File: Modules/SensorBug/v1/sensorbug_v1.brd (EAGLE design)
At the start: 41 x 30 mm, 43 parts, among them IC1 MX25R8035FZUIL0, T2 DMP3010LK3

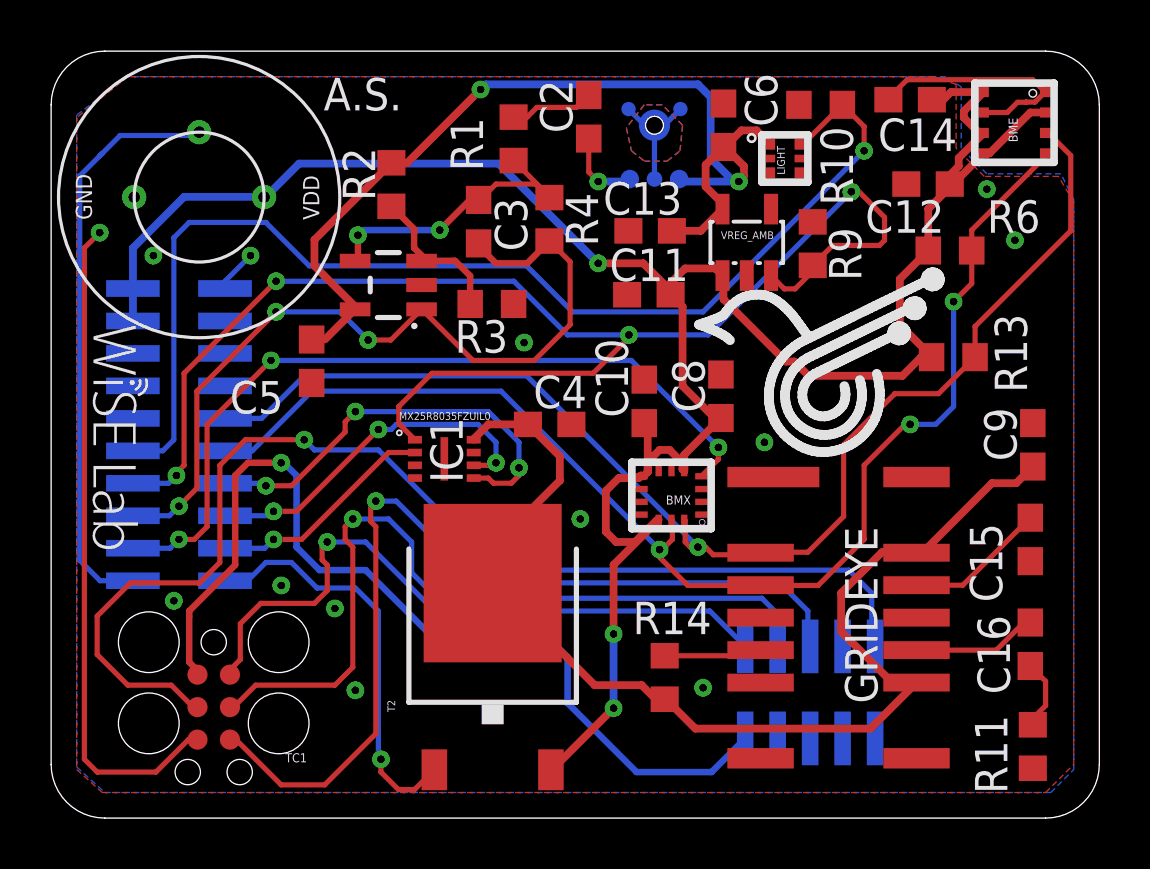
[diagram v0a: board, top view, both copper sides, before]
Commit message: Fixed Light Sensor Output
Previous light sensor output pin did not have ADC capabilities.
Interchanged DOMAIN1_EN and LIGHT_OUT.
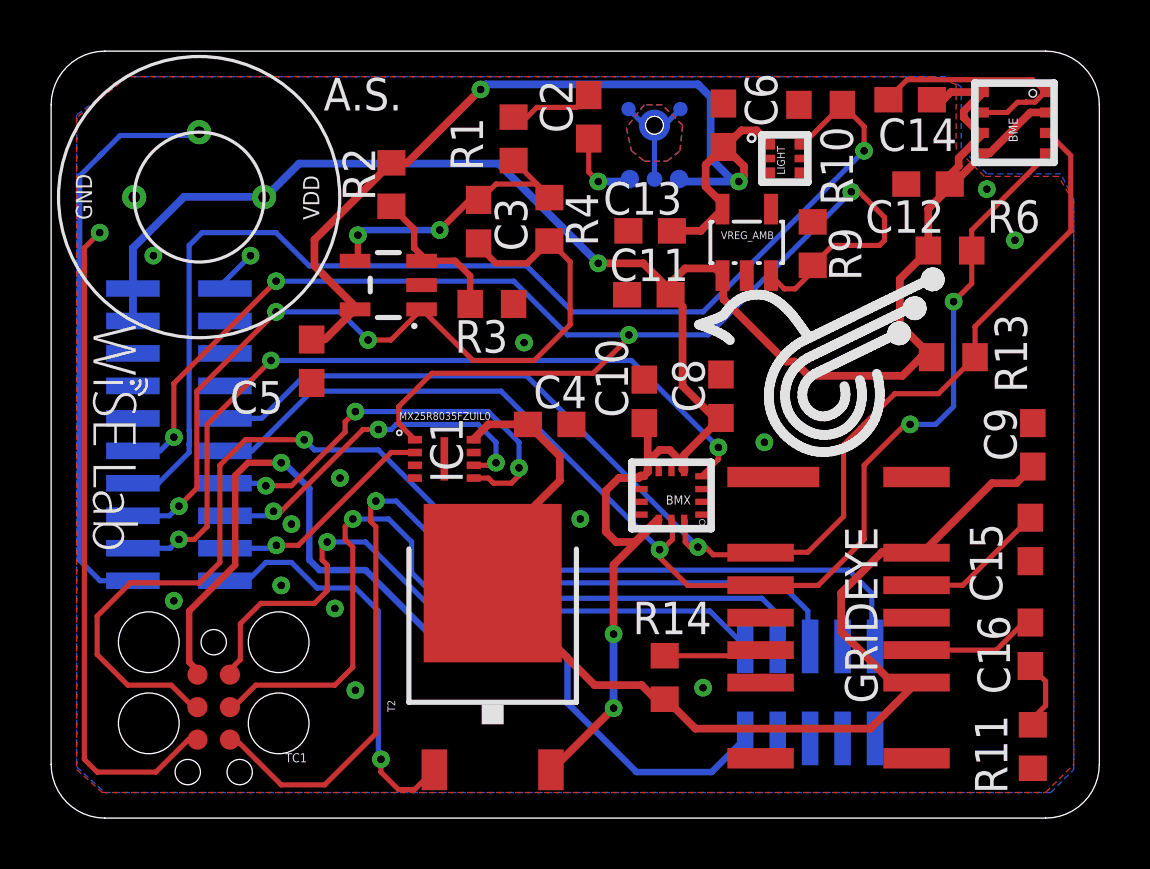
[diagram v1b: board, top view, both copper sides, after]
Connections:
- net DOMAIN1_EN: now also U$4.11; no longer U$4.13
- net LIGHT_OUT: now also U$4.13; no longer U$4.11
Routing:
- net DOMAIN1_EN: track 56.7 -> 55.2 mm
- net GND: vias 13 -> 15
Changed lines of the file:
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@@
 <layers>
 <layer number="1" name="Top" color="4" fill="1" visible="yes" active="yes"/>
-<layer number="16" name="Bottom" color="1" fill="1" visible="no" active="yes"/>
+<layer number="16" name="Bottom" color="1" fill="1" visible="yes" active="yes"/>
 <layer number="17" name="Pads" color="2" fill="1" visible="yes" active="yes"/>
 <layer number="18" name="Vias" color="2" fill="1" visible="yes" active="yes"/>
@@
 <via x="4" y="22" extent="1-16" drill="0.3"/>
 <via x="20.7" y="11.7" extent="1-16" drill="0.3"/>
+<via x="11.3" y="13.3" extent="1-16" drill="0.3"/>
+<via x="9.4" y="11.5" extent="1-16" drill="0.3"/>
 </signal>
 <signal name="SDA">
@@
 <wire x1="8.525" y1="11.825" x2="8.7" y2="12" width="0.2032" layer="16"/>
 <via x="8.7" y="12" extent="1-16" drill="0.3"/>
-<wire x1="8.7" y1="12" x2="9.6" y2="12" width="0.2032" layer="1"/>
-<wire x1="9.6" y1="12" x2="12.8" y2="15.2" width="0.2032" layer="1"/>
 <via x="12.8" y="15.2" extent="1-16" drill="0.3"/>
 <wire x1="12.8" y1="15.2" x2="13.3" y2="15.2" width="0.2032" layer="16"/>
@@
 <wire x1="17.2" y1="13.9" x2="17.1" y2="13.8" width="0.2032" layer="1"/>
 <wire x1="17.1" y1="13.8" x2="16.53" y2="13.8" width="0.2032" layer="1"/>
+<wire x1="8.7" y1="12" x2="9" y2="12" width="0.2032" layer="1"/>
+<wire x1="9" y1="12" x2="12.2" y2="15.2" width="0.2032" layer="1"/>
+<wire x1="12.2" y1="15.2" x2="12.8" y2="15.2" width="0.2032" layer="1"/>
 </signal>
 <signal name="MISO">
 <contactref element="IC1" pad="2"/>
 <contactref element="U$4" pad="18"/>
-<wire x1="6.8" y1="10.555" x2="8.355" y2="10.555" width="0.2032" layer="16"/>
-<wire x1="8.355" y1="10.555" x2="8.7" y2="10.9" width="0.2032" layer="16"/>
-<via x="8.7" y="10.9" extent="1-16" drill="0.3"/>
-<wire x1="8.7" y1="10.9" x2="9.8" y2="10.9" width="0.2032" layer="1"/>
-<wire x1="9.8" y1="10.9" x2="13.2" y2="14.3" width="0.2032" layer="1"/>
-<wire x1="13.2" y1="14.3" x2="14.23" y2="14.3" width="0.2032" layer="1"/>
+<via x="8.81" y="10.67" extent="1-16" drill="0.3"/>
+<wire x1="6.8" y1="10.555" x2="8.695" y2="10.555" width="0.2032" layer="16"/>
+<wire x1="8.695" y1="10.555" x2="8.81" y2="10.67" width="0.2032" layer="16"/>
+<wire x1="8.81" y1="10.67" x2="9.67" y2="10.67" width="0.2032" layer="1"/>
+<wire x1="9.67" y1="10.67" x2="13.3" y2="14.3" width="0.2032" layer="1"/>
+<wire x1="13.3" y1="14.3" x2="14.23" y2="14.3" width="0.2032" layer="1"/>
 </signal>
 <signal name="MOSI">
@@
 <wire x1="5.725" y1="5.61" x2="5.725" y2="5.775" width="0.254" layer="1"/>
 <wire x1="5.725" y1="5.775" x2="5.4" y2="6.1" width="0.254" layer="1"/>
-<wire x1="5.4" y1="6.1" x2="5.4" y2="7.9" width="0.254" layer="1"/>
+<wire x1="5.4" y1="6.1" x2="5.4" y2="8.1" width="0.254" layer="1"/>
 <via x="9" y="13.9" extent="1-16" drill="0.3"/>
-<wire x1="9" y1="13.9" x2="9.1" y2="13.9" width="0.254" layer="16"/>
-<wire x1="9.1" y1="13.9" x2="9.6" y2="13.4" width="0.254" layer="16"/>
-<wire x1="9.6" y1="13.4" x2="9.6" y2="10.6" width="0.254" layer="16"/>
-<wire x1="9.6" y1="10.6" x2="10.5" y2="9.7" width="0.254" layer="16"/>
-<wire x1="10.5" y1="9.7" x2="12.3" y2="9.7" width="0.254" layer="16"/>
+<wire x1="9.1" y1="13.9" x2="9" y2="13.9" width="0.254" layer="16"/>
 <wire x1="12.3" y1="9.7" x2="14.7" y2="7.3" width="0.254" layer="16"/>
 <wire x1="14.7" y1="7.3" x2="19.2" y2="7.3" width="0.254" layer="16"/>
@@
 <wire x1="22.9" y1="1.8" x2="25.8326" y2="1.8" width="0.254" layer="16"/>
 <wire x1="25.8326" y1="1.8" x2="27.1488" y2="3.1162" width="0.254" layer="16"/>
-<wire x1="5.4" y1="7.9" x2="5.4" y2="8.1" width="0.254" layer="1"/>
 <wire x1="7.2" y1="9.9" x2="5.4" y2="8.1" width="0.254" layer="1"/>
 <wire x1="7.2" y1="9.9" x2="7.2" y2="13.4" width="0.254" layer="1"/>
 <wire x1="7.2" y1="13.4" x2="7.7" y2="13.9" width="0.254" layer="1"/>
 <wire x1="7.7" y1="13.9" x2="9" y2="13.9" width="0.254" layer="1"/>
+<wire x1="9" y1="13.9" x2="9.1" y2="13.9" width="0.254" layer="16"/>
+<wire x1="9.1" y1="13.9" x2="10.1" y2="12.9" width="0.254" layer="16"/>
+<wire x1="10.1" y1="12.9" x2="10.1" y2="10.1" width="0.254" layer="16"/>
+<wire x1="10.1" y1="10.1" x2="10.5" y2="9.7" width="0.254" layer="16"/>
+<wire x1="10.5" y1="9.7" x2="12.3" y2="9.7" width="0.254" layer="16"/>
 </signal>
 <signal name="JTAG_TMS">
@@
 <wire x1="29.1" y1="20.7" x2="28.68" y2="20.7" width="0.2032" layer="1"/>
 <wire x1="28.68" y1="20.7" x2="28.16" y2="21.22" width="0.2032" layer="1"/>
-<contactref element="U$4" pad="13"/>
-<wire x1="3.2" y1="13.095" x2="4.595" y2="13.095" width="0.2032" layer="16"/>
-<wire x1="4.595" y1="13.095" x2="4.9" y2="13.4" width="0.2032" layer="16"/>
-<via x="4.9" y="13.4" extent="1-16" drill="0.3"/>
-<wire x1="4.9" y1="13.4" x2="4.9" y2="13.5" width="0.2032" layer="1"/>
-<wire x1="4.9" y1="13.5" x2="5.2" y2="13.8" width="0.2032" layer="1"/>
-<wire x1="5.2" y1="13.8" x2="5.2" y2="17.4" width="0.2032" layer="1"/>
-<wire x1="5.2" y1="17.4" x2="8.8" y2="21" width="0.2032" layer="1"/>
 <via x="8.8" y="21" extent="1-16" drill="0.3"/>
 <via x="31.3" y="24.5" extent="1-16" drill="0.3"/>
@@
 <wire x1="13.6" y1="16.1" x2="13.6" y2="15.43" width="0.2032" layer="1"/>
 <wire x1="13.6" y1="15.43" x2="14.23" y2="14.8" width="0.2032" layer="1"/>
+<contactref element="U$4" pad="11"/>
+<via x="4.8" y="14.9" extent="1-16" drill="0.3"/>
+<wire x1="3.2" y1="14.365" x2="4.265" y2="14.365" width="0.2032" layer="16"/>
+<wire x1="4.265" y1="14.365" x2="4.8" y2="14.9" width="0.2032" layer="16"/>
+<wire x1="4.8" y1="14.9" x2="4.8" y2="17" width="0.2032" layer="1"/>
+<wire x1="4.8" y1="17" x2="8.8" y2="21" width="0.2032" layer="1"/>
 </signal>
 <signal name="VREG_1">
@@
 <contactref element="LIGHT" pad="6IOUT"/>
 <contactref element="R10" pad="2"/>
-<contactref element="U$4" pad="11"/>
-<wire x1="3.2" y1="14.365" x2="4.365" y2="14.365" width="0.2032" layer="16"/>
-<wire x1="4.365" y1="14.365" x2="4.8" y2="14.8" width="0.2032" layer="16"/>
-<wire x1="4.8" y1="14.8" x2="4.8" y2="22.7" width="0.2032" layer="16"/>
-<wire x1="4.8" y1="22.7" x2="5.4" y2="23.3" width="0.2032" layer="16"/>
-<wire x1="5.4" y1="23.3" x2="8.4" y2="23.3" width="0.2032" layer="16"/>
-<wire x1="8.4" y1="23.3" x2="10.1" y2="21.6" width="0.2032" layer="16"/>
 <wire x1="10.1" y1="21.6" x2="18.6" y2="21.6" width="0.2032" layer="16"/>
 <wire x1="18.6" y1="21.6" x2="20.4" y2="19.8" width="0.2032" layer="16"/>
@@
 <wire x1="29.265" y1="26.36" x2="29.41" y2="26.36" width="0.2032" layer="1"/>
 <wire x1="29.41" y1="26.36" x2="30.95" y2="27.9" width="0.2032" layer="1"/>
+<contactref element="U$4" pad="13"/>
+<wire x1="3.2" y1="13.095" x2="4.195" y2="13.095" width="0.2032" layer="16"/>
+<wire x1="4.195" y1="13.095" x2="5.4" y2="14.3" width="0.2032" layer="16"/>
+<wire x1="5.4" y1="14.3" x2="5.4" y2="14.6" width="0.2032" layer="16"/>
+<wire x1="5.4" y1="14.6" x2="5.4" y2="14.6412875" width="0.2032" layer="16"/>
+<wire x1="5.4" y1="14.6412875" x2="5.4072" y2="14.6484875" width="0.2032" layer="16"/>
+<wire x1="5.4" y1="14.6" x2="5.4" y2="14.6412875" width="0.2032" layer="16"/>
+<wire x1="5.4" y1="14.6412875" x2="5.4072" y2="14.6484875" width="0.2032" layer="16"/>
+<wire x1="5.4072" y1="14.6484875" x2="5.4072" y2="15.1515125" width="0.2032" layer="16"/>
+<wire x1="5.4072" y1="15.1515125" x2="5.4" y2="15.1587125" width="0.2032" layer="16"/>
+<wire x1="5.4" y1="15.1587125" x2="5.4" y2="22.4" width="0.2032" layer="16"/>
+<wire x1="5.4" y1="22.4" x2="5.9" y2="22.9" width="0.2032" layer="16"/>
+<wire x1="5.9" y1="22.9" x2="8.8" y2="22.9" width="0.2032" layer="16"/>
+<wire x1="8.8" y1="22.9" x2="10.1" y2="21.6" width="0.2032" layer="16"/>
 </signal>
 <signal name="N$5">
